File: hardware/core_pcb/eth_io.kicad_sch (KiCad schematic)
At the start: 32 parts, among them J3 I/O ONLY, U6 W5500, U7 TPD4E05U06, Y4 25MHz

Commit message: Core PCB: save datasheets and clear the datasheet checks
Add hardware/datasheets with the six datasheets Gary supplied and an index.
Apply what they show: TPS54360B with 22 uH and compensation from its
datasheet, LAN8742A crystal caps 33 pF, W5500 reserved pins 38-42 left open
and its reference crystal circuit (1M, 0R), FRAM and choke checks cleared.

Co-Authored-By: Claude Opus 5.5 (1M context) <noreply@anthropic.com>
Claude-Session: https://claude.ai/code/session_014onnq3eRiDkqdAB6fKiRDW
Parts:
- added R62: 1M, Resistor_SMD:R_0603_1608Metric, symbol Device:R
- added R63: 0R, Resistor_SMD:R_0603_1608Metric, symbol Device:R
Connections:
- net GND: no longer U6.38 (RSVD), U6.39 (RSVD), U6.40 (RSVD), U6.41 (RSVD), U6.42 (RSVD)
- net W5500_XI: now also R62.1
- net W5500_XO: now also R62.2, R63.1; no longer C61.1, Y4.3
- new net W5500_XTAL2: C61.1, R63.2, Y4.3
- no-connect marks 16 -> 21
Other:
- note added: "C60: W5500 reference circuit R62: W5500 reference circuit R63: drive-level option, W5500 reference circuit R51: series, at the MCU R52: series, at the MCU C64: TX centre tap J3: I/O boards only; silkscreen I/O ONLY R60: link LED; W5500 LED outputs sink (active low) R61: activity LED"
- note added: "Notes U6: PMODE[2:0] internal pull-ups = all capable, auto-negotiation; RSVD pin 23 to ground, RSVD 38-42 NC; VBG open. No auto-MDIX: the I/O board's LAN8742A does HP auto-MDIX, so a straight cable works C51: one per AVDD pin C52: one per AVDD pin C53: one per AVDD pin C54: one per AVDD pin C55: one per AVDD pin C56: one per AVDD pin C57: VDD pin 28 Y4: own crystal, CL 18 pF, +/-30 ppm (W5500 dat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"
- note removed: "Notes U6: PMODE[2:0] internal pull-ups = all capable, auto-negotiation; RSVD pins to ground; VBG open C51: one per AVDD pin C52: one per AVDD pin C53: one per AVDD pin C54: one per AVDD pin C55: one per AVDD pin C56: one per AVDD pin C57: VDD pin 28"
- note removed: "Y4: own crystal, separate from the MCU's HSE C60: CHECK for the crystal's CL R51: series, at the MCU R52: series, at the MCU C64: TX centre tap J3: I/O boards only; silkscreen I/O ONLY R60: link LED; W5500 LED outputs sink (active low) R61: activity LED"
- moved on the sheet: C60, C61, C62, C63, C64, J3, R51, R52, R53, R54, R55, R56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

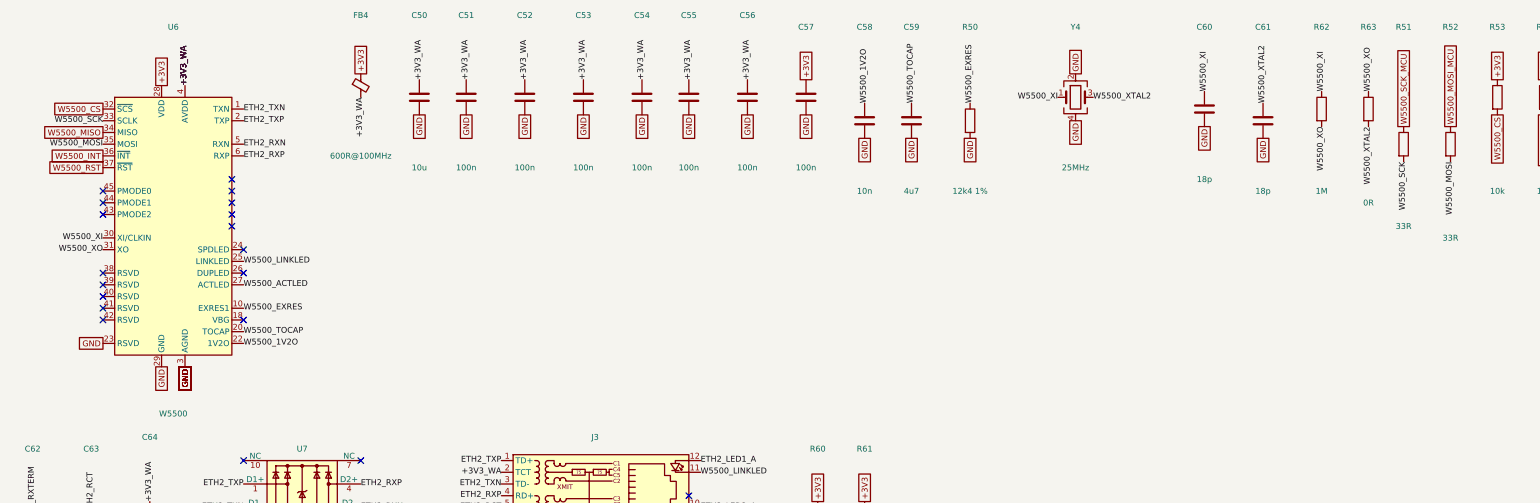
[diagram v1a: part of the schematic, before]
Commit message: CORE PCB rev 0.2: I/O node section on the same board
Three new sheets: field digital I/O with the hardware output gate (ISO2H823V2.5,
ISO808A-1, ISO1I813T), field power / pump / relay coils / USB-C, and the isolated
analog (AD4112) and temperature (ADS124S08) islands. Project symbols for the six
I/O chips missing from KiCad. SPI4 nets renamed: the bus is shared with the I/O chips.
423 parts, netlist check passes. CORE_PCB.md: pin map, connectors, BOM, section 14.

Co-Authored-By: Claude Opus 5.5 <noreply@anthropic.com>
Claude-Session: https://claude.ai/code/session_014onnq3eRiDkqdAB6fKiRDW
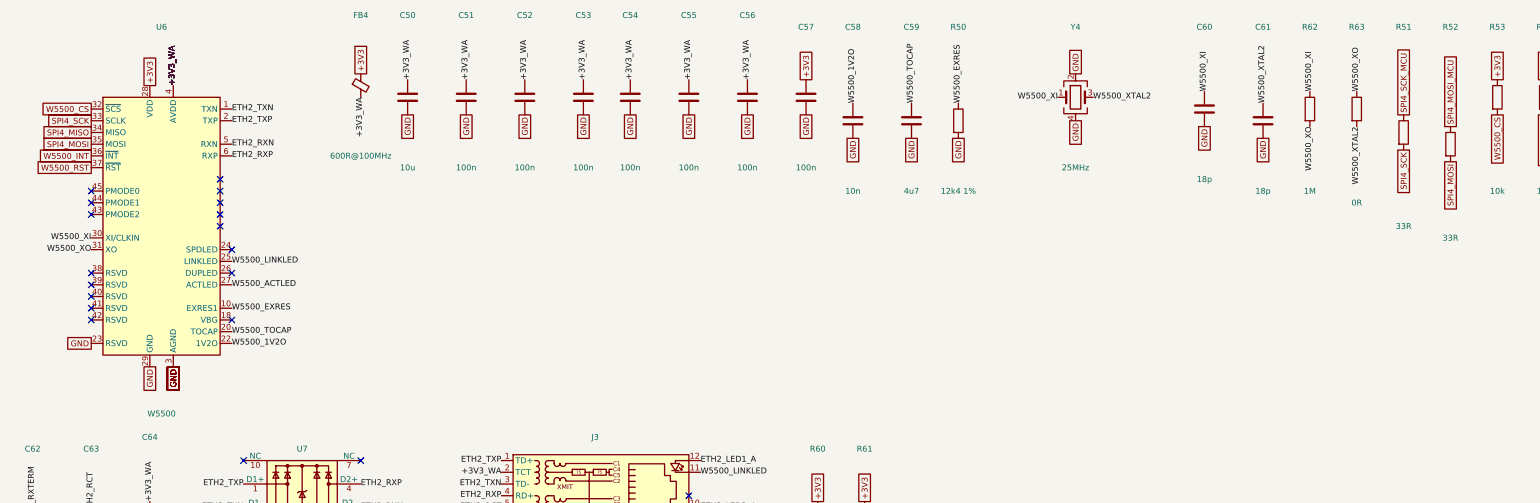
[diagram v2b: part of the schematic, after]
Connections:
- net W5500_MISO renamed SPI4_MISO
- net W5500_MOSI renamed SPI4_MOSI
- net W5500_MOSI_MCU renamed SPI4_MOSI_MCU
- net W5500_SCK renamed SPI4_SCK
- net W5500_SCK_MCU renamed SPI4_SCK_MCU
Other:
- moved on the sheet: C50, C54, C58, R50, R51, R62, R63, U6
